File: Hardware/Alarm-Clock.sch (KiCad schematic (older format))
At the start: 26 parts, among them IC1 MEGA8-AI, Q1 16Mhz, X1 MINI-USB-32005-201

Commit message: update schematic and board
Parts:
- removed JP11: PINHD-1X4, Alarm-Clock:1X04, symbol Alarm-Clock-eagle-import:PINHD-1X4
- D1, D2: value 1N4148DO35-7 -> 1N4148
- JP13, JP7, JP8, JP9: value PINHD-1X1 -> PIN
- JP4: value PINHD-1X10 -> RTC
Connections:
- net GND: now also C1.2, C2.2, DIS1.1 (GND), DIS1.16 (NC@2), DIS1.5 (R/W), IC1.3 (GND@1), IC1.5 (GND@2), JP13.1, JP2.7, JP4.3, R3.2, S1.1 (S), S1.2 (S1), S2.1 (S), S2.2 (S1), S3.1 (S), S3.2 (S1), S4.1 (S), S4.2 (S1), X1.5
- net VCC: now reaches D2.A, DIS1.2 (VCC), JP2.1, JP4.4, R6.1, X1.1
- net VCC: now also R5.1; no longer R5.2
- net PC4: now reaches IC1.27 (PC4(ADC4/SDA)), JP4.5
- net PC5: now reaches IC1.28 (PC5(ADC5/SCL)), JP4.6
- net PD3: now reaches IC1.1 (PD3(INT1)), R2.1
- net PB0: now reaches DIS1.11 (D4), IC1.12 (PB0(ICP))
- net PB1: now reaches DIS1.12 (D5), IC1.13 (PB1(OC1A))
- net PB2: now reaches DIS1.13 (D6), IC1.14 (PB2(SS/OC1B))
- net PB3: now reaches DIS1.14 (D7), IC1.15 (PB3(MOSI/OC2))
- net PB4: now reaches DIS1.6 (E), IC1.16 (PB4(MISO))
- net PB5: now reaches DIS1.4 (RS), IC1.17 (PB5(SCK))
- net VUSB: now reaches D1.C, IC1.18 (AVCC), IC1.4 (VCC@1), IC1.6 (VCC@2), R4.1
- net PD4: now reaches IC1.2 (PD4(XCK/T0)), JP1.1
- net PC0: now reaches IC1.23 (PC0(ADC0)), S4.3 (P), S4.4 (P1)
- net PC1: now reaches IC1.24 (PC1(ADC1)), S3.3 (P), S3.4 (P1)
- net PC2: now reaches IC1.25 (PC2(ADC2)), S2.3 (P), S2.4 (P1)
- net PC3: now reaches IC1.26 (PC3(ADC3)), S1.3 (P), S1.4 (P1)
- net PD0: now reaches IC1.30 (PD0(RXD)), JP2.3
- net PD1: now reaches IC1.31 (PD1(TXD)), JP2.2
- net PD2: now reaches IC1.32 (PD2(INT0)), R1.1
- net at DIS1.3 (CONTR): now also R5.2; no longer R5.1
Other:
- note added: "DFPlayer"
- note added: "Display"
- note added: "Inputs"
- note added: "Microcontroller"
- note added: "RTC module"
- note added: "USB"
- moved on the sheet: C1, C2, D1, D2, DIS1, IC1, JP1, JP13, JP2, JP4, JP7, JP8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

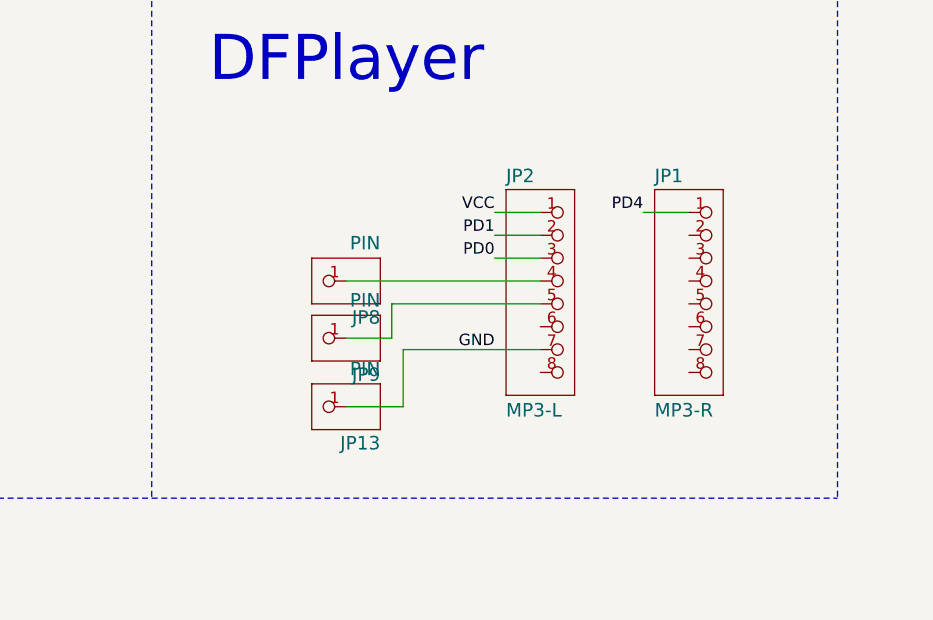
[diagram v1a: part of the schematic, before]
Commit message: Added 3d models to board
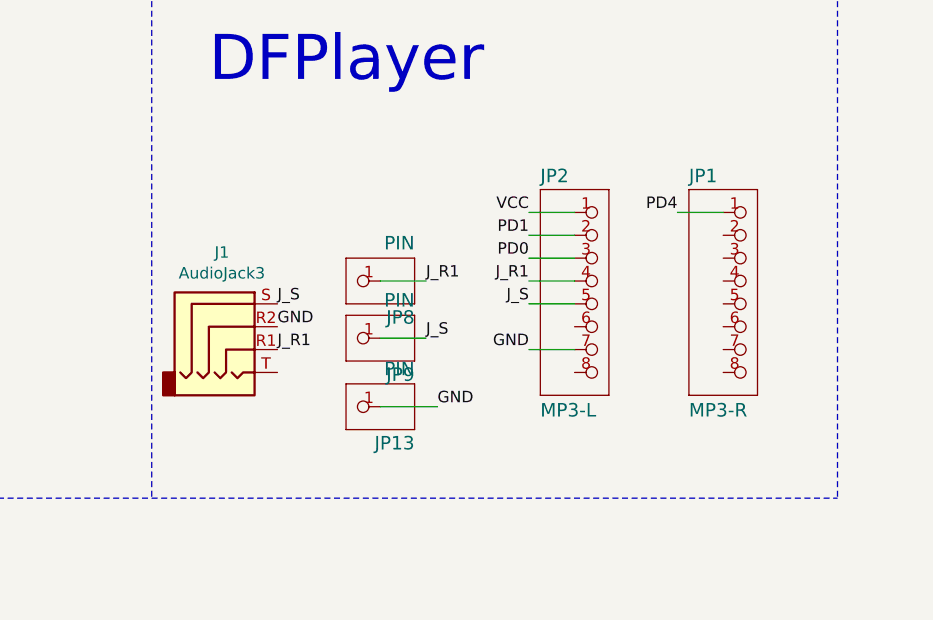
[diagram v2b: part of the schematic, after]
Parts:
- added J1: AudioJack3, Alarm-Clock:Jack_3.5mm_PJ320D_Horizontal, symbol Connector:AudioJack4
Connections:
- net GND: now also J1.R2
- net J_R1: now reaches JP2.4, JP8.1
- net J_R1: now also J1.R1
- net J_S: now reaches JP2.5, JP9.1
- net J_S: now also J1.S
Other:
- moved on the sheet: JP1, JP13, JP2, JP8, JP9
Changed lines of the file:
@@
 	8200 1350 8200 1400
 Wire Wire Line
-	4850 3150 4650 3150
+	5000 3150 4800 3150
 Wire Wire Line
 	1400 3100 1150 3100
@@
 	1400 3000 1150 3000
 Wire Wire Line
-	4000 4000 4250 4000
+	4150 4000 4400 4000
 Wire Wire Line
 	750  1200 750  1300
@@
 	2750 1300 2650 1300
 Wire Wire Line
-	4850 3250 4650 3250
-Wire Wire Line
-	4850 3350 4650 3350
+	5000 3250 4800 3250
+Wire Wire Line
+	5000 3350 4800 3350
 Wire Wire Line
 	2300 5350 1900 5350
@@
 	9500 1350 9500 1500
 Wire Wire Line
-	4850 3450 4000 3450
-Wire Wire Line
-	4000 3700 4200 3700
-Wire Wire Line
-	4200 3700 4200 3550
-Wire Wire Line
-	4200 3550 4850 3550
+	4150 3700 4350 3700
+Wire Wire Line
+	4800 3550 5000 3550
 $Comp
 L Alarm-Clock-eagle-import:MEGA8-AI IC1
@@
 L Alarm-Clock-eagle-import:PINHD-1X8 JP1
 U 1 1 9FA72D5F
-P 5600 3550
-F 0 "JP1" H 5350 4075 59  0000 L BNN
-F 1 "MP3-R" H 5350 3050 59  0000 L BNN
-F 2 "Alarm-Clock:1X08" H 5600 3550 50  0001 C CNN
-F 3 "" H 5600 3550 50  0001 C CNN
-	1    5600 3550
+P 5750 3550
+F 0 "JP1" H 5500 4075 59  0000 L BNN
+F 1 "MP3-R" H 5500 3050 59  0000 L BNN
+F 2 "Alarm-Clock:1X08" H 5750 3550 50  0001 C CNN
+F 3 "" H 5750 3550 50  0001 C CNN
+	1    5750 3550
 	1    0    0    -1
 $EndComp
@@
 L Alarm-Clock-eagle-import:PINHD-1X8 JP2
 U 1 1 83BD4EC0
-P 4950 3550
-F 0 "JP2" H 4700 4075 59  0000 L BNN
-F 1 "MP3-L" H 4700 3050 59  0000 L BNN
-F 2 "Alarm-Clock:1X08" H 4950 3550 50  0001 C CNN
-F 3 "" H 4950 3550 50  0001 C CNN
-	1    4950 3550
+P 5100 3550
+F 0 "JP2" H 4850 4075 59  0000 L BNN
+F 1 "MP3-L" H 4850 3050 59  0000 L BNN
+F 2 "Alarm-Clock:1X08" H 5100 3550 50  0001 C CNN
+F 3 "" H 5100 3550 50  0001 C CNN
+	1    5100 3550
 	1    0    0    -1
 $EndComp
@@
 L Alarm-Clock-eagle-import:PINHD-1X1 JP8
 U 1 1 357D3C8D
-P 3900 3450
-F 0 "JP8" H 3650 3575 59  0000 L BNN
-F 1 "PIN" H 3650 3250 59  0000 L BNN
-F 2 "Alarm-Clock:1X01" H 3900 3450 50  0001 C CNN
-F 3 "" H 3900 3450 50  0001 C CNN
-	1    3900 3450
+P 4050 3450
+F 0 "JP8" H 3800 3575 59  0000 L BNN
+F 1 "PIN" H 3800 3250 59  0000 L BNN
+F 2 "Alarm-Clock:1X01" H 4050 3450 50  0001 C CNN
+F 3 "" H 4050 3450 50  0001 C CNN
+	1    4050 3450
 	-1   0    0    1
 $EndComp
@@
 L Alarm-Clock-eagle-import:PINHD-1X1 JP9
 U 1 1 C8B46213
-P 3900 3700
-F 0 "JP9" H 3650 3825 59  0000 L BNN
-F 1 "PIN" H 3650 3500 59  0000 L BNN
-F 2 "Alarm-Clock:1X01" H 3900 3700 50  0001 C CNN
-F 3 "" H 3900 3700 50  0001 C CNN
-	1    3900 3700
+P 4050 3700
+F 0 "JP9" H 3800 3825 59  0000 L BNN
+F 1 "PIN" H 3800 3500 59  0000 L BNN
+F 2 "Alarm-Clock:1X01" H 4050 3700 50  0001 C CNN
+F 3 "" H 4050 3700 50  0001 C CNN
+	1    4050 3700
 	-1   0    0    1
 $EndComp
@@
 L Alarm-Clock-eagle-import:PINHD-1X1 JP13
 U 1 1 9B8C9E68
-P 3900 4000
-F 0 "JP13" H 3650 4125 59  0000 L BNN
-F 1 "PIN" H 3650 3800 59  0000 L BNN
-F 2 "Alarm-Clock:1X01" H 3900 4000 50  0001 C CNN
-F 3 "" H 3900 4000 50  0001 C CNN
-	1    3900 4000
+P 4050 4000
+F 0 "JP13" H 3800 4125 59  0000 L BNN
+F 1 "PIN" H 3800 3800 59  0000 L BNN
+F 2 "Alarm-Clock:1X01" H 4050 4000 50  0001 C CNN
+F 3 "" H 4050 4000 50  0001 C CNN
+	1    4050 4000
 	-1   0    0    1
 $EndComp
@@
 Text Label 4200 6350 0    50   ~ 0
 PD1
-Text Label 4650 3250 2    50   ~ 0
+Text Label 4800 3250 2    50   ~ 0
 PD1
-Text Label 4650 3350 2    50   ~ 0
+Text Label 4800 3350 2    50   ~ 0
 PD0
 Text Label 4200 6250 0    50   ~ 0
@@
 Text Label 4200 6650 0    50   ~ 0
 PD4
-Text Label 5300 3150 2    50   ~ 0
+Text Label 5450 3150 2    50   ~ 0
 PD4
 Wire Wire Line
-	5300 3150 5500 3150
+	5450 3150 5650 3150
 Wire Wire Line
 	9100 1350 9100 1400
@@
 Text Label 1150 3000 2    50   ~ 0
 GND
-Text Label 4650 3750 2    50   ~ 0
+Text Label 4800 3750 2    50   ~ 0
 GND
 Text Label 2250 6550 2    50   ~ 0
@@
 Text Label 8500 1400 3    50   ~ 0
 GND
-Text Label 4650 3150 2    50   ~ 0
+Text Label 4800 3150 2    50   ~ 0
 VCC
 Text Label 1150 3100 2    50   ~ 0
@@
 	3150 0    3150 4400
 Wire Wire Line
-	4250 4000 4250 3750
-Wire Wire Line
-	4250 3750 4850 3750
+	4800 3750 5000 3750
 Text Notes 3400 2600 0    197  ~ 0
 DFPlayer
@@
 Text Notes 300  4850 0    197  ~ 0
 Microcontroller
+$Comp
+L Connector:AudioJack4 J1
+U 1 1 61AD099A
+P 3500 3650
+F 0 "J1" H 3457 3975 50  0000 C CNN
+F 1 "AudioJack3" H 3457 3884 50  0000 C CNN
+F 2 "Alarm-Clock:Jack_3.5mm_PJ320D_Horizontal" H 3500 3650 50  0001 C CNN
+F 3 "~" H 3500 3650 50  0001 C CNN
+	1    3500 3650
+	1    0    0    -1
+$EndComp
+Text Label 3700 3650 0    50   ~ 0
+GND
+Text Label 4400 4000 0    50   ~ 0
+GND
+Text Label 3700 3750 0    50   ~ 0
+J_R1
+Text Label 3700 3550 0    50   ~ 0
+J_S
+Text Label 4350 3700 0    50   ~ 0
+J_S
+Wire Wire Line
+	4350 3450 4150 3450
+Text Label 4800 3450 2    50   ~ 0
+J_R1
+Wire Wire Line
+	5000 3450 4800 3450
+Text Label 4350 3450 0    50   ~ 0
+J_R1
+Text Label 4800 3550 2    50   ~ 0
+J_S
 $EndSCHEMATC
